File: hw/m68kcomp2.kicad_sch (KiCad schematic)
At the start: 36 parts, among them U2 74HC393, U3 74HC10, U4 74HC148, U5 mc68030rc, U7 mc68881, U9 GAL16V8, X1 25.175MHz

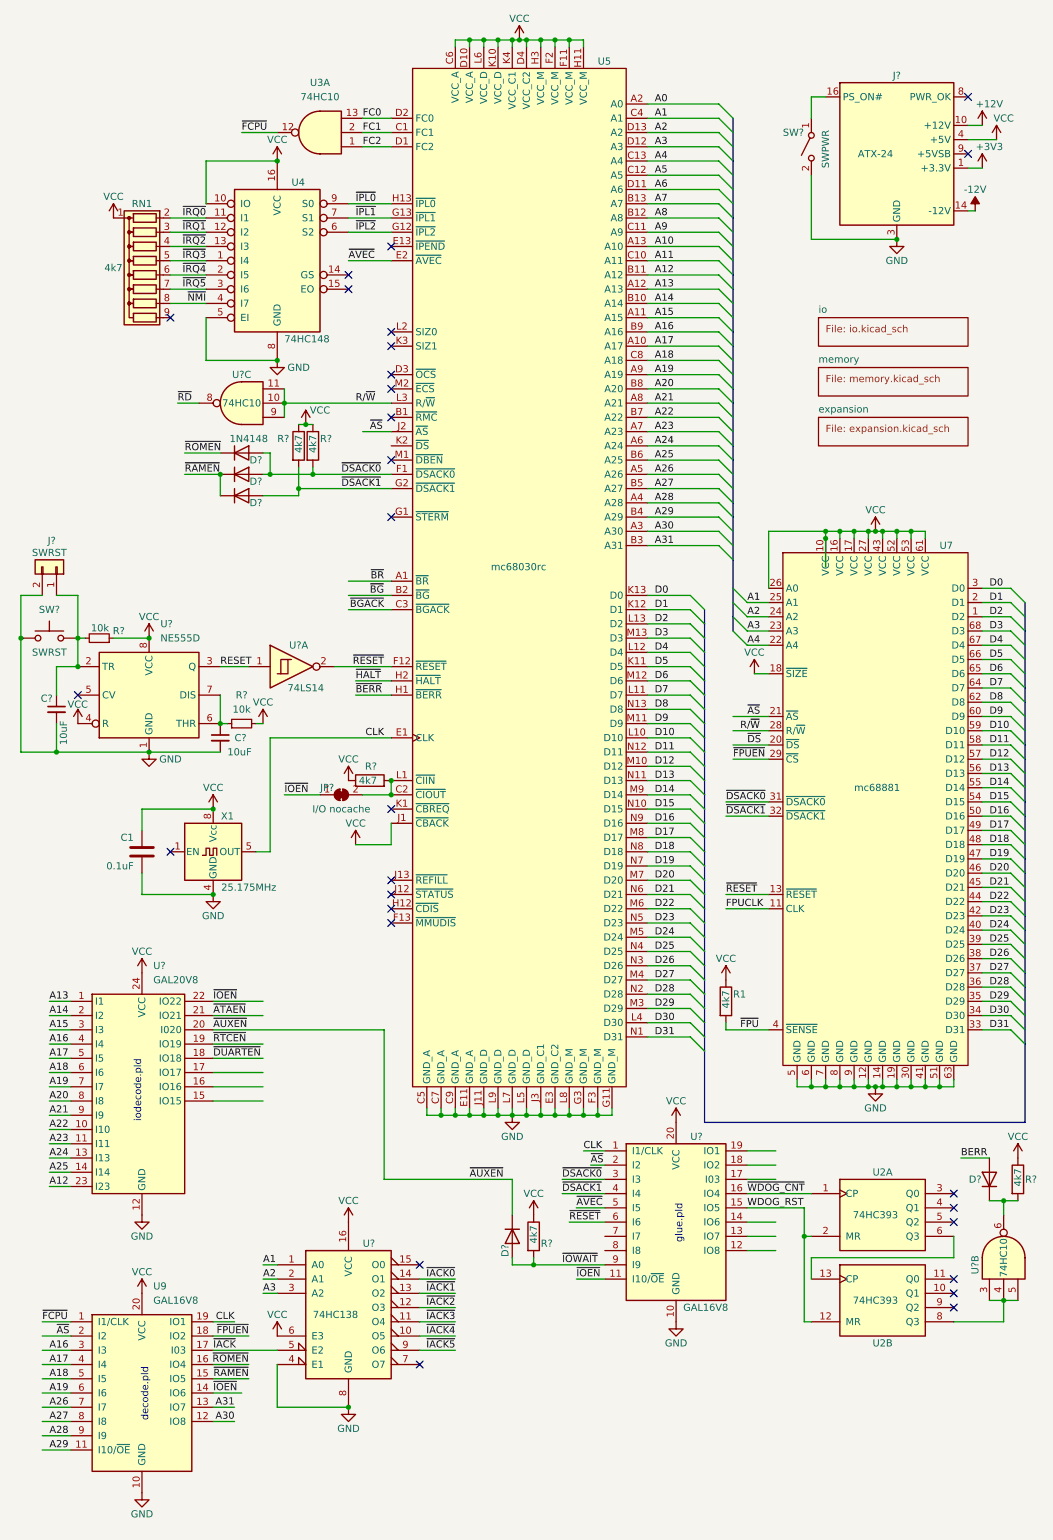
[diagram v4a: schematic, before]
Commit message: separate power sheet
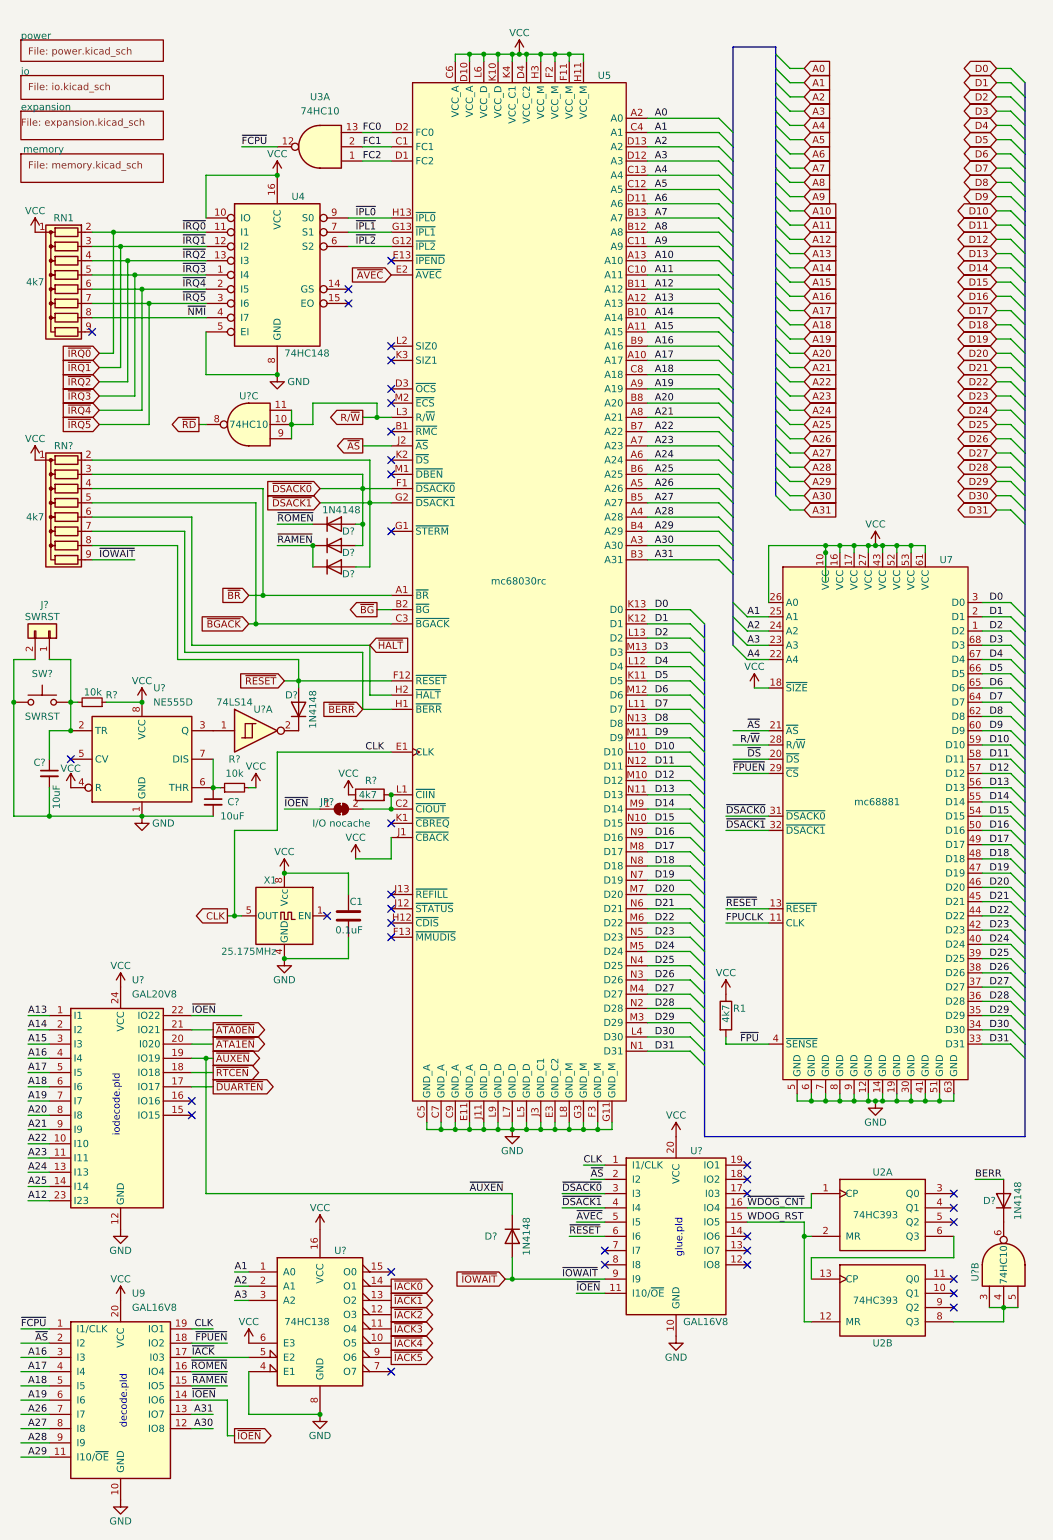
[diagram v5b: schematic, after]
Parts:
- removed J?: ATX-24, symbol Connector:ATX-24
- removed R? (x4): 4k7, OptoDevice:R_LDR_D13.8mm_P9.0mm_Vertical, symbol Device:R
- removed SW?: SWPWR, symbol Switch:SW_SPST
- added D?: 1N4148, Diode_THT:D_DO-35_SOD27_P7.62mm_Horizontal, symbol Diode:1N4148
- added RN?: 4k7, Resistor_THT:R_Array_SIP9, symbol Device:R_Network08
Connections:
- net VCC: now also RN?.1 (common)
- net ~{AUXEN}: now also U?.19 (IO19); no longer U?.20 (I020)
- net ~{BERR}: now also RN?.7 (R6)
- net ~{BGACK}: now also RN?.5 (R4)
- net ~{BR}: now also RN?.4 (R3)
- net ~{DSACK0}: now also RN?.3 (R2)
- net ~{DSACK1}: now also RN?.2 (R1)
- net ~{DUARTEN}: now also U?.17 (IO17); no longer U?.18 (IO18)
- net ~{HALT}: now also RN?.6 (R5)
- net ~{IOWAIT}: now also RN?.9 (R8)
- net ~{RESET}: now also D?.2 (A), RN?.8 (R7); no longer U?.2
- net ~{RTCEN}: now also U?.18 (IO18); no longer U?.19 (IO19)
- net RESET: no longer names the net of U?.1, U?.3 (Q)
- net ~{ATAEN} renamed ~{ATA0EN}
- new net: D?.1 (K), U?.2
- new net ~{ATA1EN}: U?.20 (I020)
- no-connect marks 28 -> 37
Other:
- added sheet power (power.kicad_sch)
- moved on the sheet: C1, C?, D?, J?, JP?, R1, R?, RN1, SW?, U3A, U4, U5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

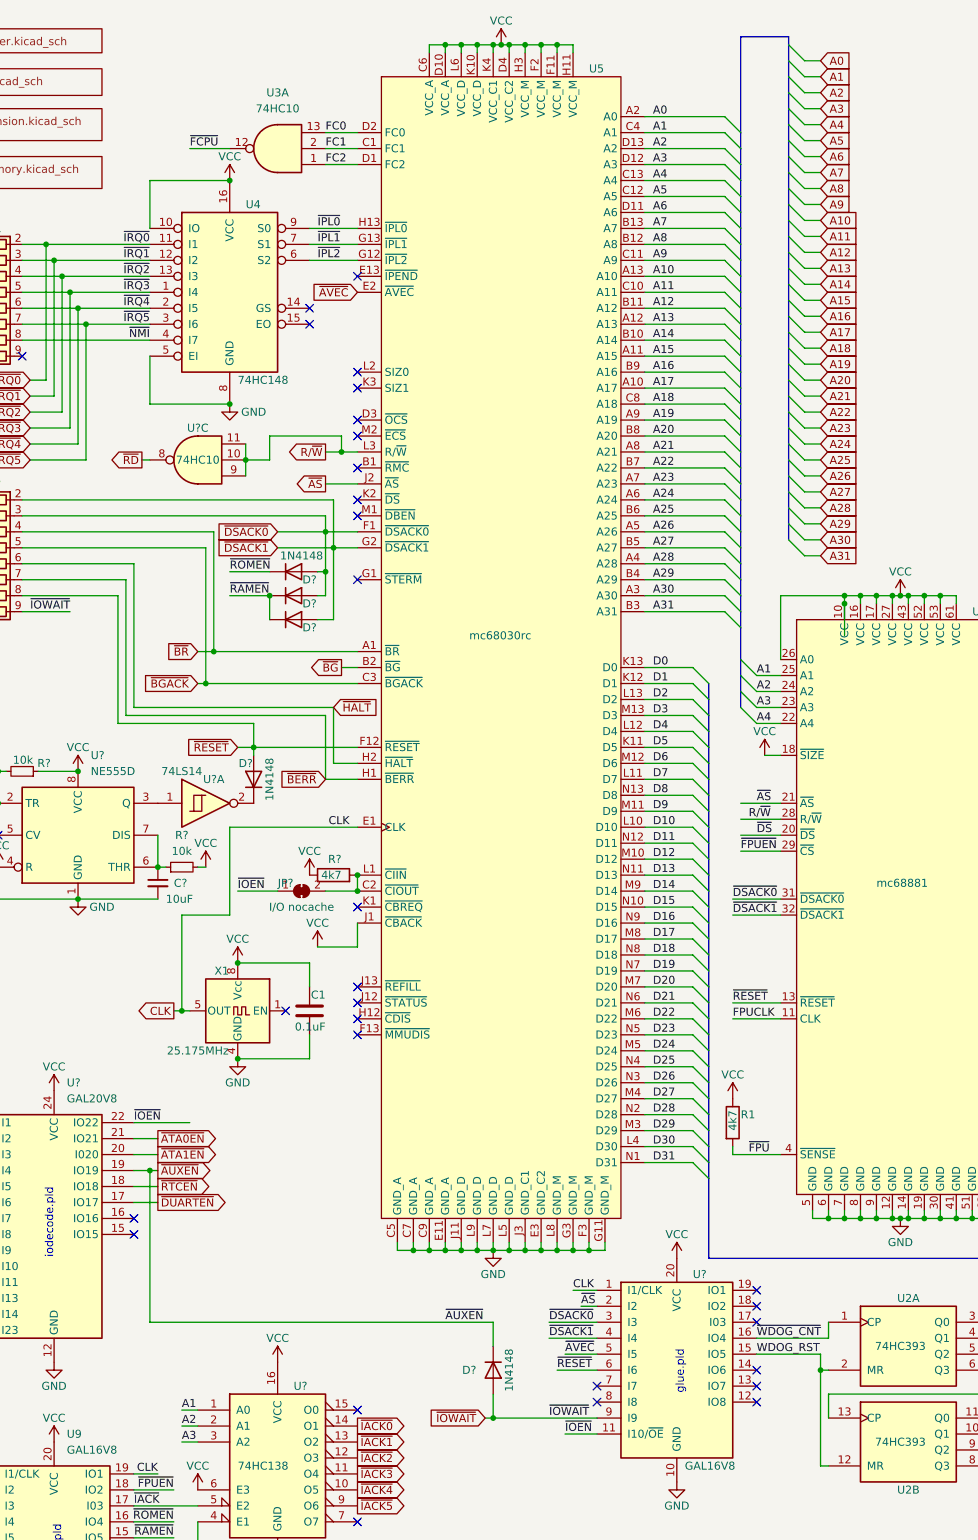
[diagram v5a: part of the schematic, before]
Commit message: decoupling, test points, and ATA0EN/ATA1EN in iodecode.pld
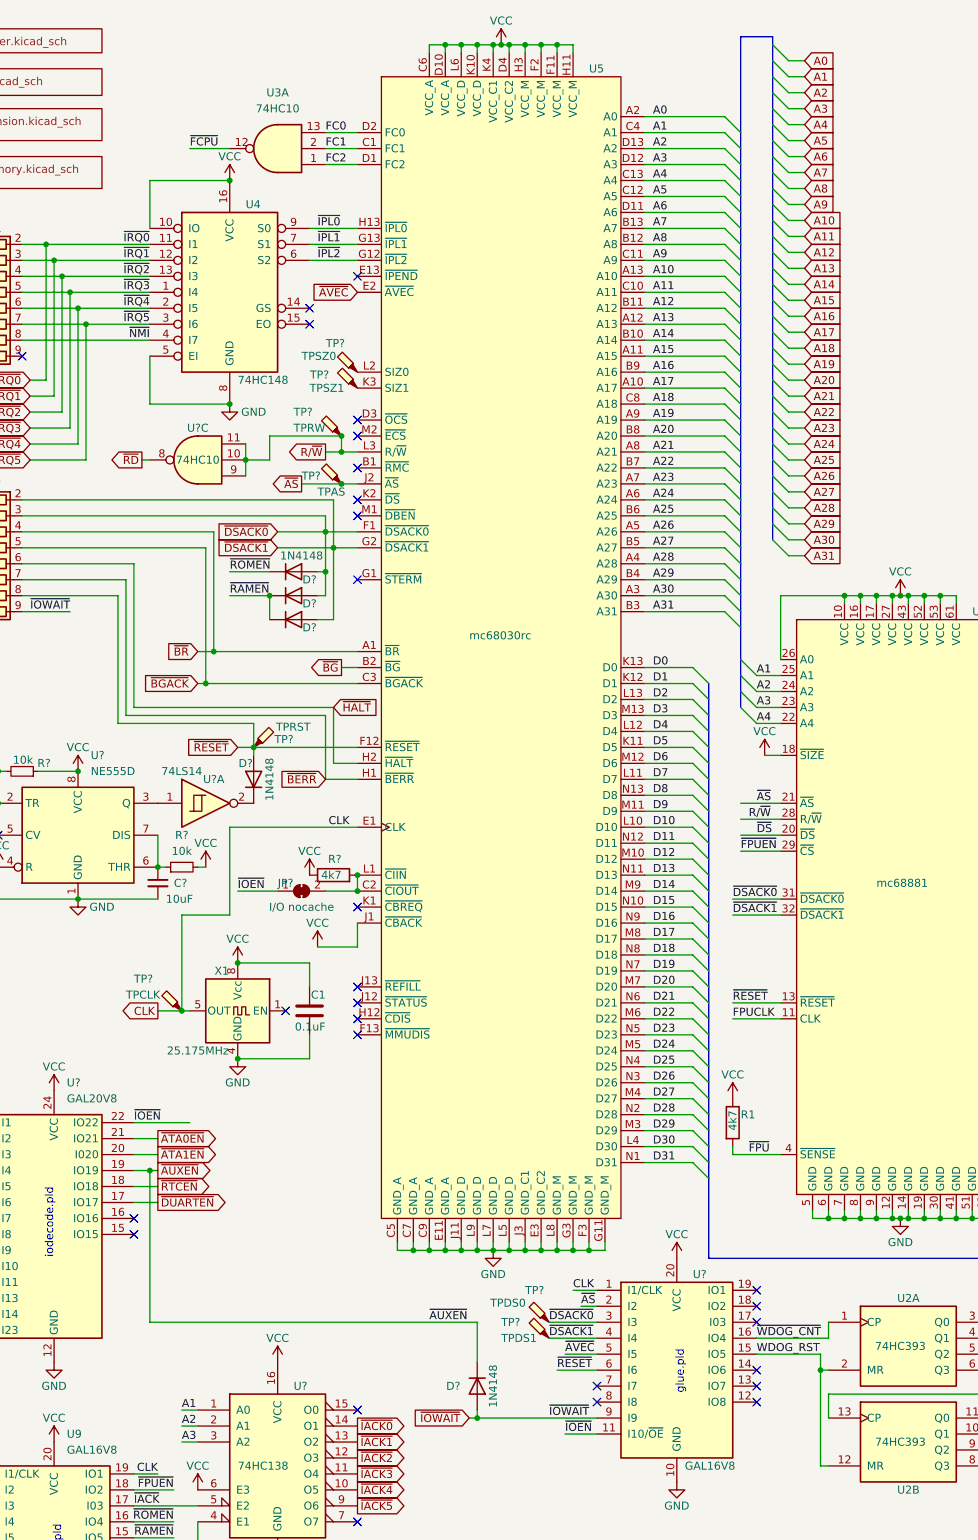
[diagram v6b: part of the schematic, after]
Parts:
- added TP?: TPRST, symbol Connector:TestPoint_Probe
- added TP?: TPSZ0, symbol Connector:TestPoint_Probe
- added TP?: TPAS, symbol Connector:TestPoint_Probe
- added TP?: TPSZ1, symbol Connector:TestPoint_Probe
- added TP?: TPDS0, symbol Connector:TestPoint_Probe
- added TP?: TPCLK, symbol Connector:TestPoint_Probe
- added TP?: TPRW, symbol Connector:TestPoint_Probe
- added TP?: TPDS1, symbol Connector:TestPoint_Probe
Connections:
- net CLK: now also TP?.1
- net R/~{W}: now also TP?.1
- net ~{AS}: now also TP?.1
- net ~{DSACK0}: now also TP?.1
- net ~{DSACK1}: now also TP?.1
- net ~{RESET}: now also TP?.1
- net at U5.K3 (SIZ1): now also TP?.1
- net at U5.L2 (SIZ0): now also TP?.1
- no-connect marks 37 -> 35
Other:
- moved on the sheet: D?

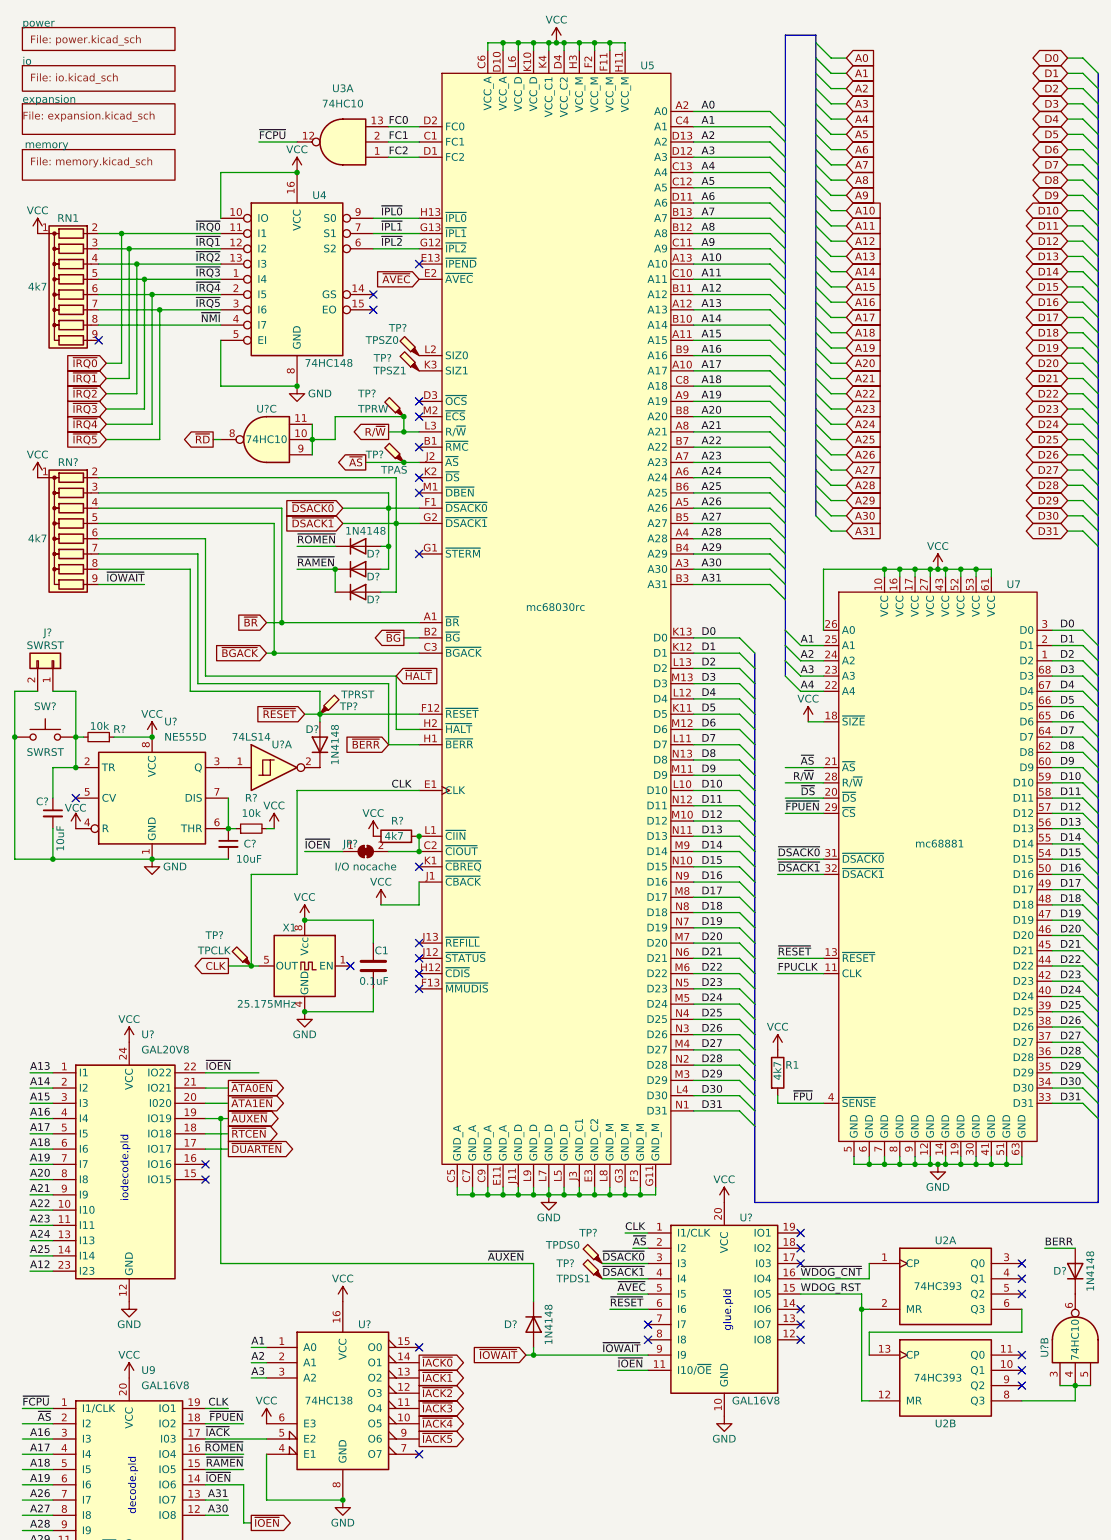
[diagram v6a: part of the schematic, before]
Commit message: fixed ERC errors
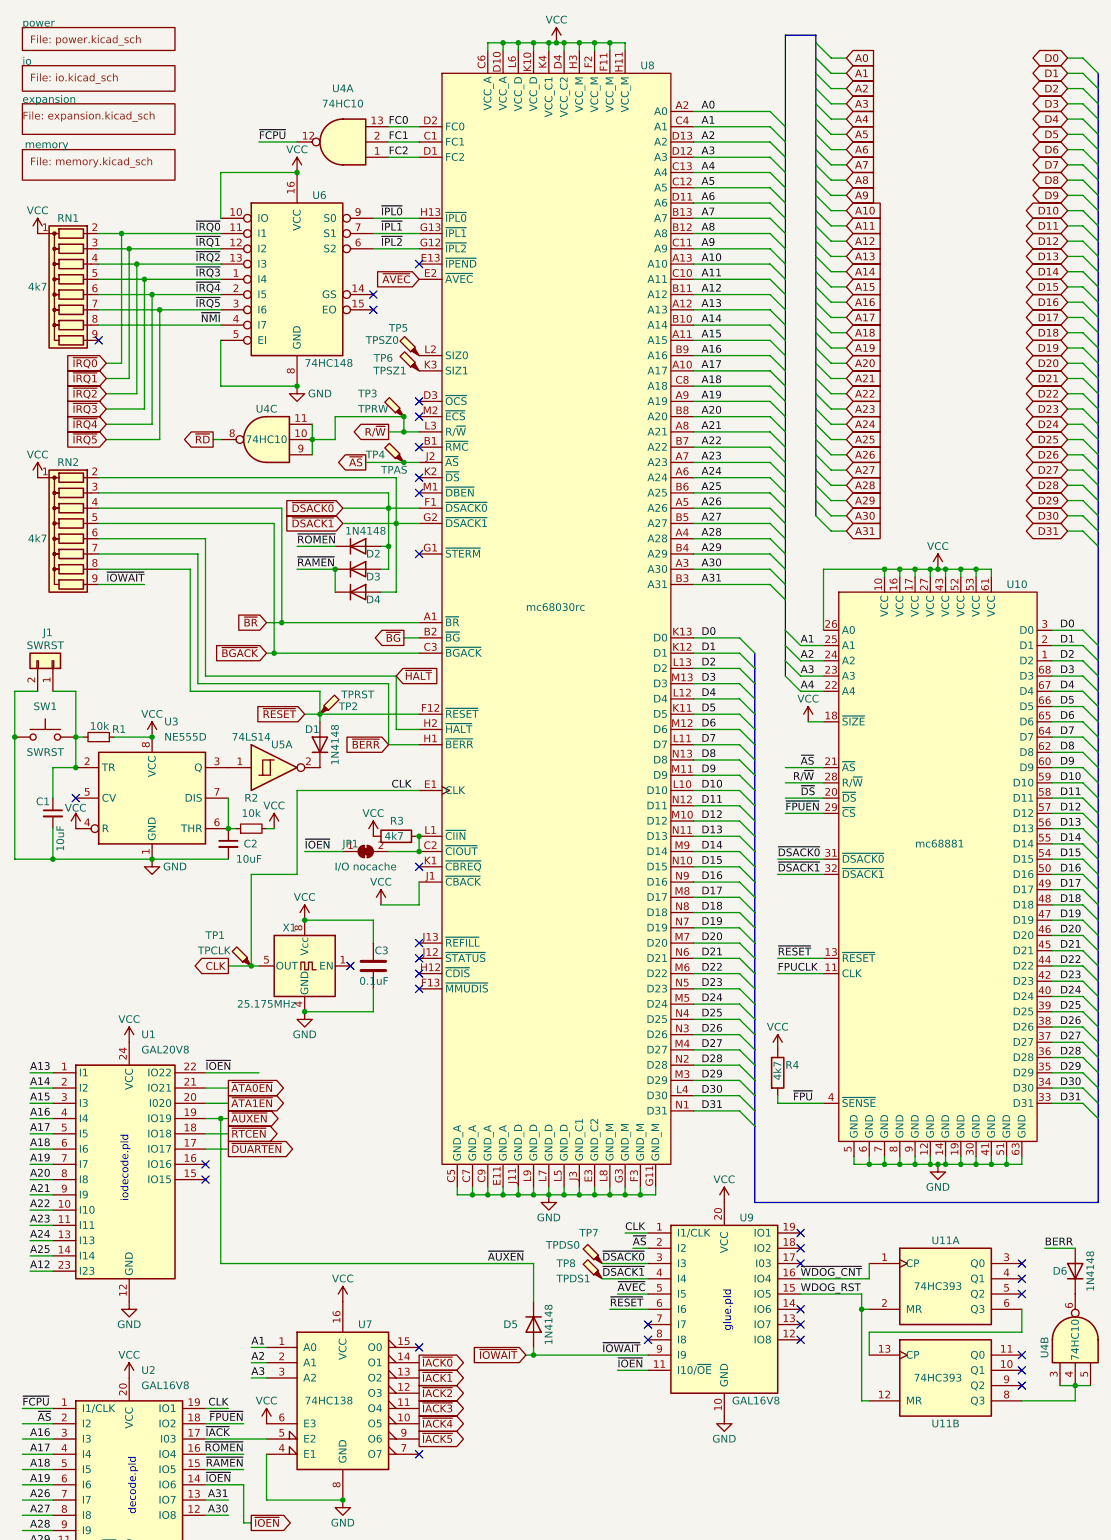
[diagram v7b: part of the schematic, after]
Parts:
- gave numbers to parts that had none: 29
- renumbered C1 to C3, R1 to R4, U7 to U10, U2 to U11, U9 to U2, U3 to U4, U4 to U6, U5 to U8

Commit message: first pass at assigning footprints
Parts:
- J1: footprint (none) -> Connector_PinHeader_2.54mm:PinHeader_1x02_P2.54mm_Vertical
- JP1: footprint (none) -> Jumper:SolderJumper-2_P1.3mm_Bridged_RoundedPad1.0x1.5mm
- R1, R2: footprint (none) -> Resistor_SMD:R_0805_2012Metric_Pad1.20x1.40mm_HandSolder
- TP1, TP2, TP3, TP4, TP5, TP6, TP7, TP8: footprint (none) -> TestPoint:TestPoint_Pad_D1.5mm
- U1: footprint (none) -> Package_DIP:DIP-24_W7.62mm_Socket
- U10: footprint Package_LCC:PLCC-68 -> Package_LCC:PLCC-68_THT-Socket
- U5: footprint (none) -> Package_SO:SO-14_3.9x8.65mm_P1.27mm
- U7: footprint (none) -> Package_SO:SO-16_3.9x9.9mm_P1.27mm
